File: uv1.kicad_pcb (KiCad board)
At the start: 2 copper layers, 54.9 x 63 mm, 14 parts, among them J1 Conn_02x06_Odd_Even, J2 Conn_01x02, U1 TC7106, U2 LCD-A2X1C50TR

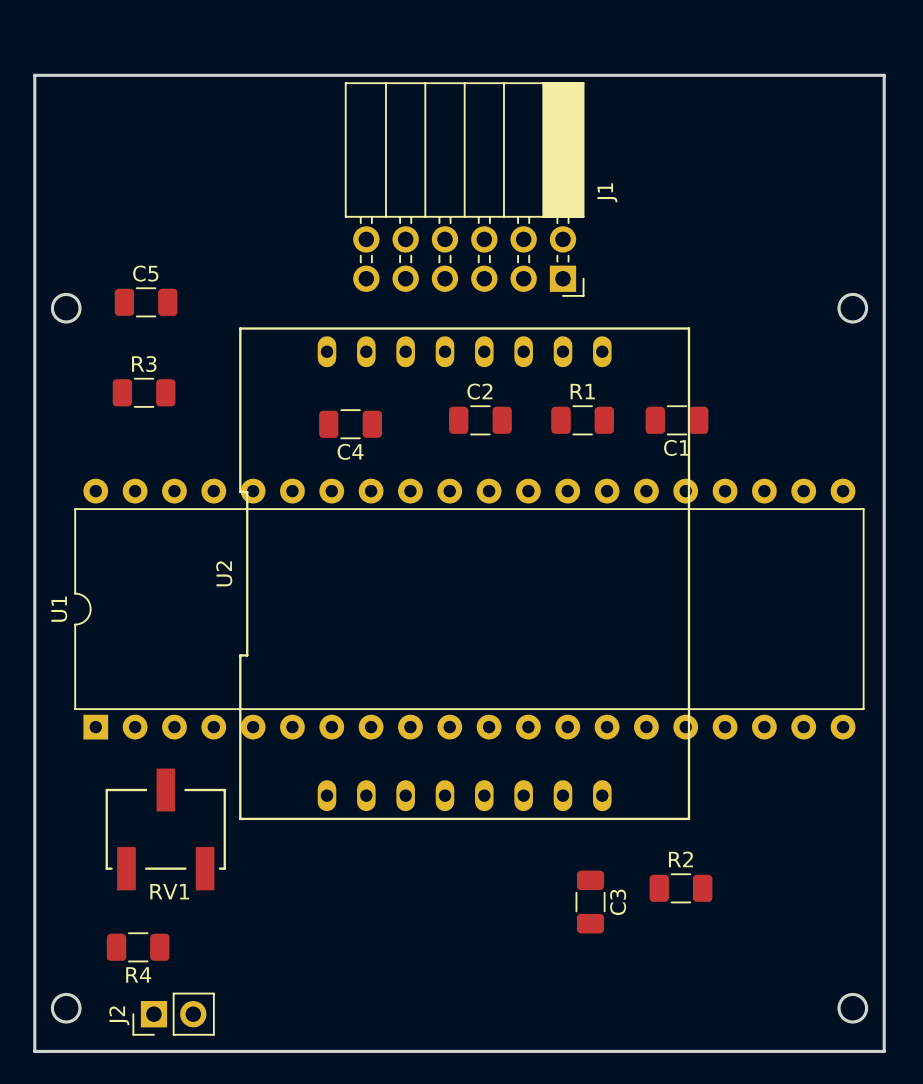
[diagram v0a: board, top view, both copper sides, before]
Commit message: Display DE151 Sensor connector 2x 2x2 male
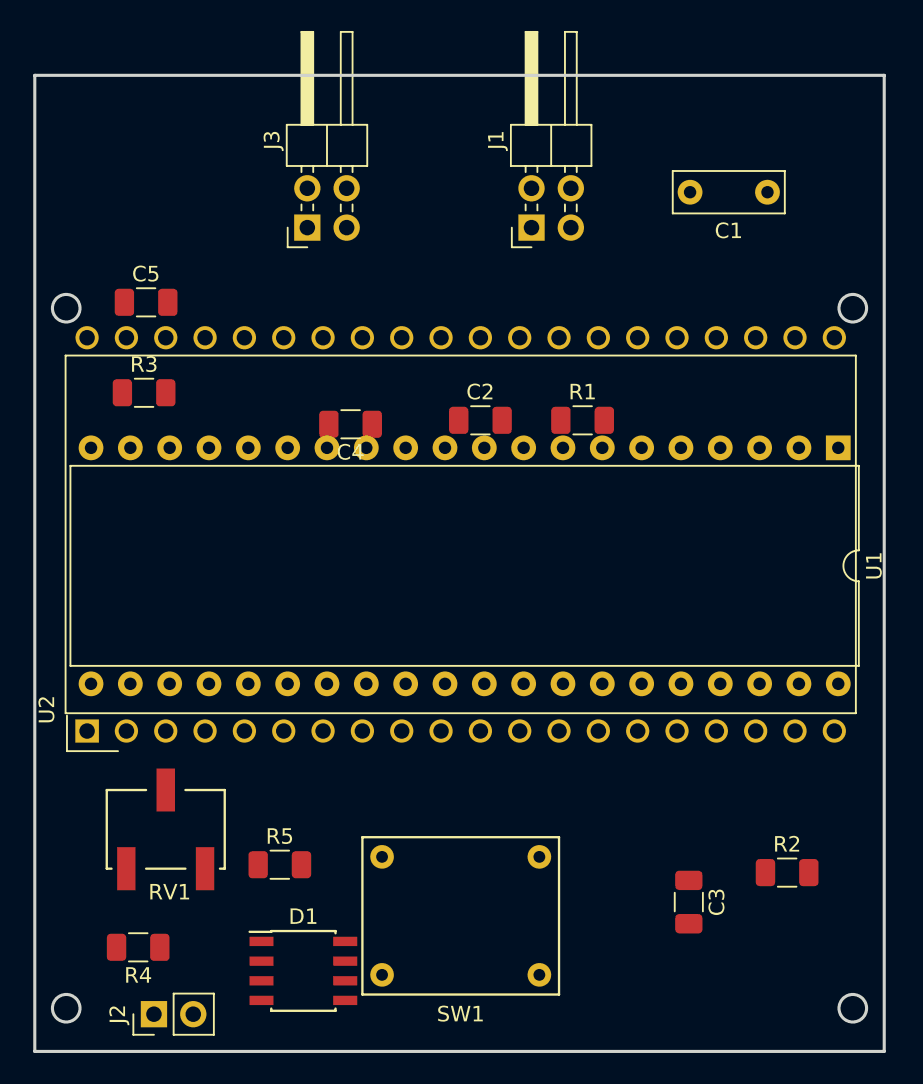
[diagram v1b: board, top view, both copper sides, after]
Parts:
- added D1: LM285D-1.2, Package_SO:SOIC-8_3.9x4.9mm_P1.27mm, F.Cu at (89.4, 139.7)
- added J3: Conn_02x02_Odd_Even, Connector_PinHeader_2.54mm:PinHeader_2x02_P2.54mm_Horizontal, F.Cu at (89.7, 91.7)
- added R5: 2.2k, Resistor_SMD:R_1206_3216Metric, F.Cu at (87.9, 132.8)
- added SW1: SW_Push, uv1:MEC_3FTH9, F.Cu at (99.6, 136.1)
- C1: footprint Capacitor_SMD:C_1206_3216Metric -> Capacitor_THT:C_Rect_L7.0mm_W2.5mm_P5.00mm
- J1: value Conn_02x06_Odd_Even -> Conn_02x02_Odd_Even; footprint Connector_PinSocket_2.54mm:PinSocket_2x06_P2.54mm_Horizontal -> Connector_PinHeader_2.54mm:PinHeader_2x02_P2.54mm_Horizontal
- R4: value 24k -> 6.8k
- RV1: value 1k -> 20k
- U2: value LCD-A2X1C50TR -> DE151-RS-20; footprint uv1:LCD-A2X1C50TR -> uv1:DE151-RS-20
- moved U1 51.2 mm to (124.0, 105.9), turned to 270 degrees
- moved U2 26.4 mm to (75.4, 124.2), turned to 90 degrees
- moved C1 15.8 mm to (119.4, 89.4)
- moved R2 6.93 mm to (120.7, 133.3)
- moved C3 6.35 mm to (114.3, 135.3)
- moved J1 3.88 mm to (104.1, 91.7), turned to 90 degrees
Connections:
- J1 pad 3: Net-(J1-Pad3) -> +9V
- J1 pad 4: Net-(J1-Pad3) -> +9V
- R2 pad 2: Net-(J1-Pad3) -> Net-(J3-Pad1)
- R4 pad 1: +9V -> Net-(R4-Pad1)
- U1 pad 1: +9V -> Net-(R4-Pad1)
- U1 pad 10: /3C -> /LCD_3C
- U1 pad 11: /3B -> /LCD_3B
- U1 pad 12: /3A -> /LCD_3A
- U1 pad 13: /3F -> /LCD_3F
- U1 pad 14: /3E -> /LCD_3E
- U1 pad 15: /2D -> /LCD_2D
- U1 pad 16: /2B -> /LCD_2B
- U1 pad 17: /2F -> /LCD_2F
- U1 pad 18: /2E -> /LCD_2E
- U1 pad 19: /1BC -> /LCD_1BC
- U1 pad 2: Net-(U1-Pad2) -> /LCD_4D
- U1 pad 20: Net-(U1-Pad20) -> /LCD_-
- U1 pad 21: /BP -> /LCD_BP
- U1 pad 22: /2G -> /LCD_2G
- U1 pad 23: /2A -> /LCD_2A
- U1 pad 24: /2C -> /LCD_2C
- U1 pad 25: /3G -> /LCD_3G
- U1 pad 3: Net-(U1-Pad3) -> /LCD_4C
- U1 pad 4: Net-(U1-Pad4) -> /LCD_4B
- U1 pad 5: Net-(U1-Pad5) -> /LCD_4A
- U1 pad 6: Net-(U1-Pad6) -> /LCD_4F
- U1 pad 7: Net-(U1-Pad7) -> /LCD_4G
- U1 pad 8: Net-(U1-Pad8) -> /LCD_4E
- U1 pad 9: /3D -> /LCD_3D
- U2 pad 1: /1BC -> /LCD_BP
- U2 pad 10: /2B -> /LCD_2D
- U2 pad 11: /2A -> /LCD_2C
- U2 pad 12: /2F -> /LCD_BP
- U2 pad 13: /2G -> /LCD_3E
- U2 pad 14: /2E -> /LCD_3D
- U2 pad 15: /2D -> /LCD_3C
- U2 pad 16: /BP -> /LCD_DP3
- U2 pad 2: /3F -> /LCD_-
- U2 pad 3: /3G -> /LCD_1BC
- U2 pad 4: /3E -> Net-(U2-Pad4)
- U2 pad 5: /3D -> Net-(U2-Pad5)
- U2 pad 6: /3C -> Net-(U2-Pad6)
- U2 pad 7: /3B -> Net-(U2-Pad7)
- U2 pad 8: /3A -> /LCD_BP
- U2 pad 9: /2C -> /LCD_2E

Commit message: DE115 LCD with new footprint + 3D
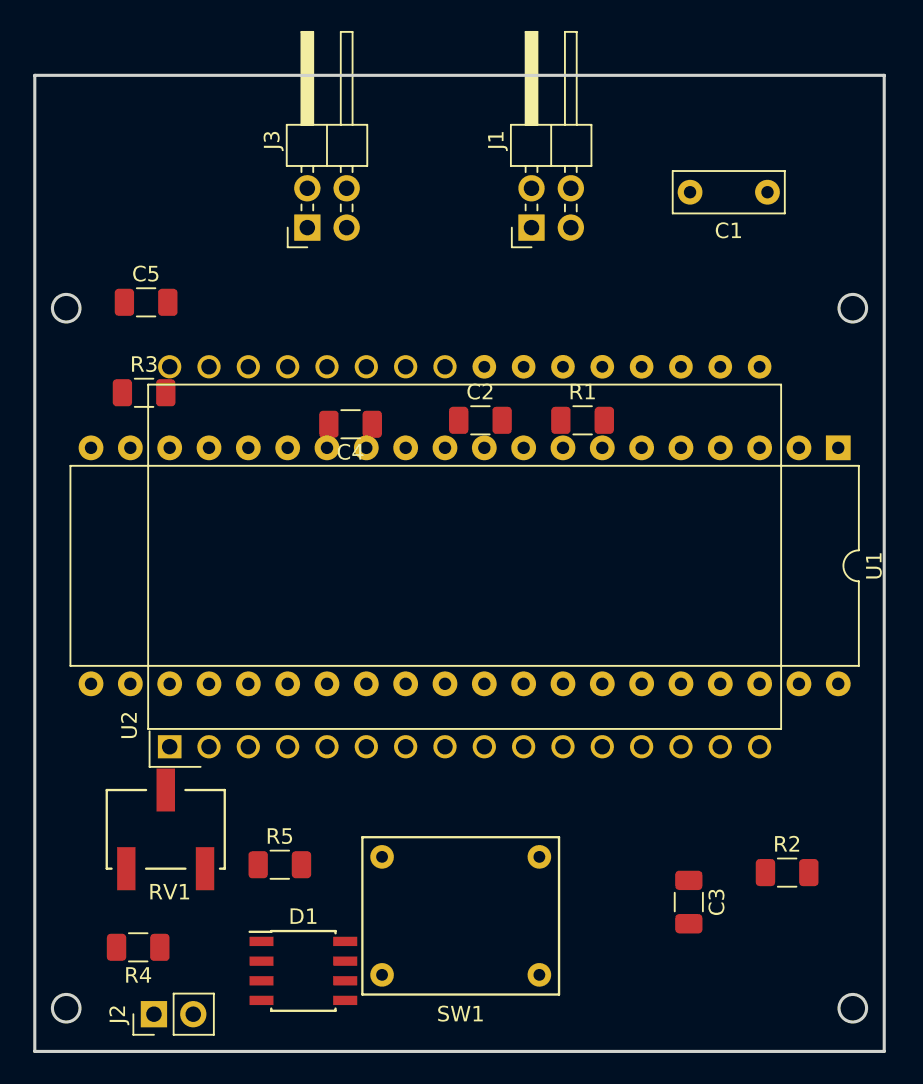
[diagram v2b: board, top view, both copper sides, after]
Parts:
- U2: value DE151-RS-20 -> DE115-RS-20; footprint uv1:DE151-RS-20 -> uv1:DE115-RS-20
- moved U2 5.43 mm to (80.8, 125.2)
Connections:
- U1 pad 10: /LCD_3C -> /LCD_2C
- U1 pad 11: /LCD_3B -> /LCD_2B
- U1 pad 12: /LCD_3A -> /LCD_2A
- U1 pad 13: /LCD_3F -> /LCD_2F
- U1 pad 14: /LCD_3E -> /LCD_2E
- U1 pad 15: /LCD_2D -> /LCD_1D
- U1 pad 16: /LCD_2B -> /LCD_1B
- U1 pad 17: /LCD_2F -> /LCD_1F
- U1 pad 18: /LCD_2E -> /LCD_1E
- U1 pad 2: /LCD_4D -> /LCD_3D
- U1 pad 22: /LCD_2G -> /LCD_1G
- U1 pad 23: /LCD_2A -> /LCD_1A
- U1 pad 24: /LCD_2C -> /LCD_1C
- U1 pad 25: /LCD_3G -> /LCD_2G
- U1 pad 3: /LCD_4C -> /LCD_3C
- U1 pad 4: /LCD_4B -> /LCD_3B
- U1 pad 5: /LCD_4A -> /LCD_3A
- U1 pad 6: /LCD_4F -> /LCD_3F
- U1 pad 7: /LCD_4G -> /LCD_3G
- U1 pad 8: /LCD_4E -> /LCD_3E
- U1 pad 9: /LCD_3D -> /LCD_2D
- U2 pad 12: /LCD_BP -> /LCD_DP3
- U2 pad 16: /LCD_DP3 -> /LCD_3B
- U2 pad 17: /LCD_4E -> (no net)
- U2 pad 18: /LCD_4D -> (no net)
- U2 pad 19: /LCD_4C -> (no net)
- U2 pad 20: /LCD_4B -> (no net)
- U2 pad 21: /LCD_4A -> (no net)
- U2 pad 22: /LCD_4F -> (no net)
- U2 pad 23: /LCD_4G -> (no net)
- U2 pad 24: /LCD_3B -> (no net)
- U2 pad 25: /LCD_3A -> /LCD_1A
- U2 pad 26: /LCD_3F -> /LCD_1F
- U2 pad 27: /LCD_3G -> /LCD_1G
- U2 pad 28: /LCD_BP -> (no net)
- U2 pad 29: /LCD_2B -> (no net)
- U2 pad 30: /LCD_2A -> /LCD_BP
- U2 pad 31: /LCD_2F -> /LCD_BP
- U2 pad 32: /LCD_2G -> /LCD_BP
- U2 pad 4: Net-(U2-Pad4) -> /LCD_BP
- U2 pad 5: Net-(U2-Pad5) -> /LCD_1E
- U2 pad 6: Net-(U2-Pad6) -> /LCD_1D
- U2 pad 7: Net-(U2-Pad7) -> /LCD_1C

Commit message: 2x7 sensor connector
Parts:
- removed J3: Conn_02x02_Odd_Even, Connector_PinHeader_2.54mm:PinHeader_2x02_P2.54mm_Horizontal
- removed R5: 2.2k, Resistor_SMD:R_1206_3216Metric
- J1: value Conn_02x02_Odd_Even -> Conn_02x07_Odd_Even; footprint Connector_PinHeader_2.54mm:PinHeader_2x02_P2.54mm_Horizontal -> Connector_PinSocket_2.54mm:PinSocket_2x07_P2.54mm_Horizontal
- moved C4 33.6 mm to (109.5, 133.3), turned to 0 degrees
- moved C2 28.0 mm to (89.2, 129.5)
- moved R1 12.7 mm to (115.3, 94.2)
- moved C5 10.5 mm to (80.3, 86.1)
- moved R3 9.97 mm to (80.3, 92.5)
- moved J1 4.49 mm to (107.2, 95.0), turned to 270 degrees
- moved C3 3.82 mm to (115.3, 131.6)
- moved R2 2.93 mm to (121.5, 130.6)
- moved U1 2.84 mm to (123.4, 103.1)
- moved U2 2.03 mm to (80.8, 123.2)
- moved RV1 1.48 mm to (79.2, 129.8)
- moved R4 1.05 mm to (77.7, 138.4)
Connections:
- R2 pad 2: Net-(J3-Pad1) -> Net-(J1-Pad11)
- U2 pad 17: (no net) -> /LCD_3A
- U2 pad 18: (no net) -> /LCD_3F
- U2 pad 19: (no net) -> /LCD_3G
- U2 pad 20: (no net) -> /LCD_2B
- U2 pad 21: (no net) -> /LCD_2A
- U2 pad 22: (no net) -> /LCD_2F
- U2 pad 23: (no net) -> /LCD_2G
- U2 pad 24: (no net) -> /LCD_1B

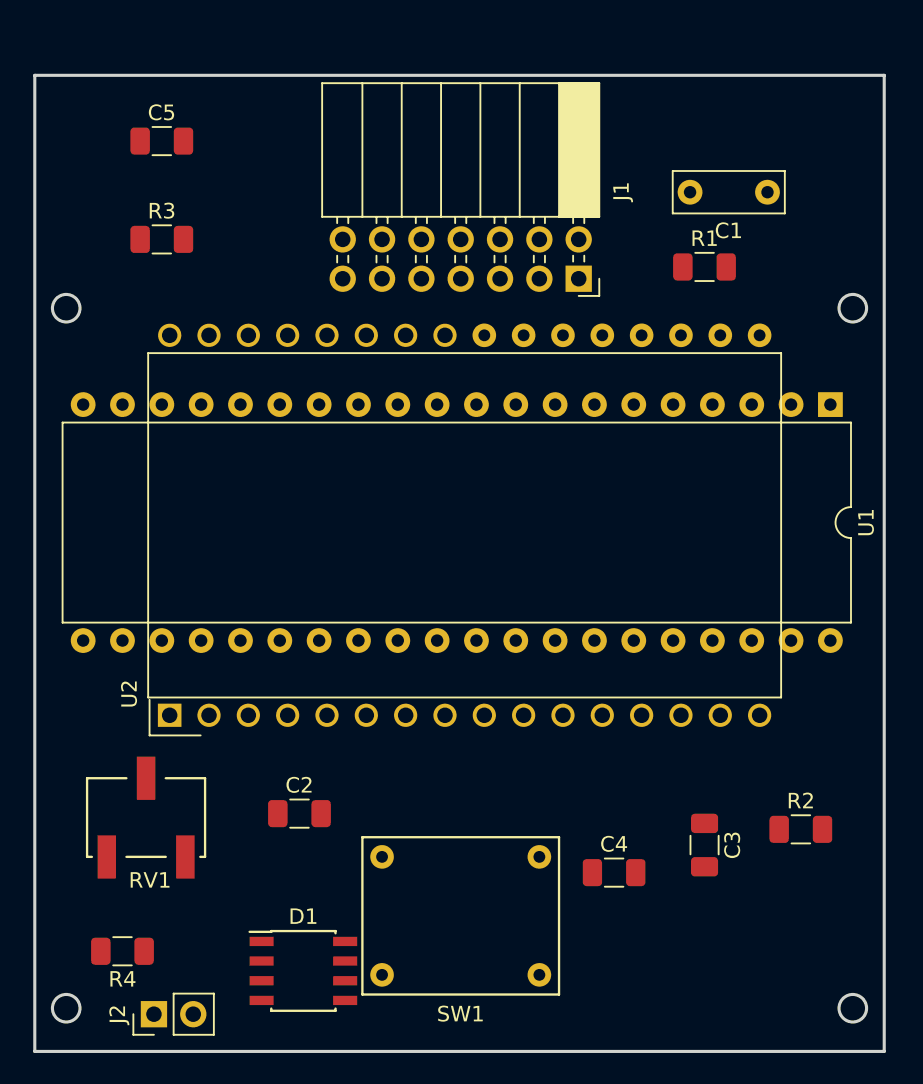
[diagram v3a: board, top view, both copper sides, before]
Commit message: Updated 3d model of LCD again
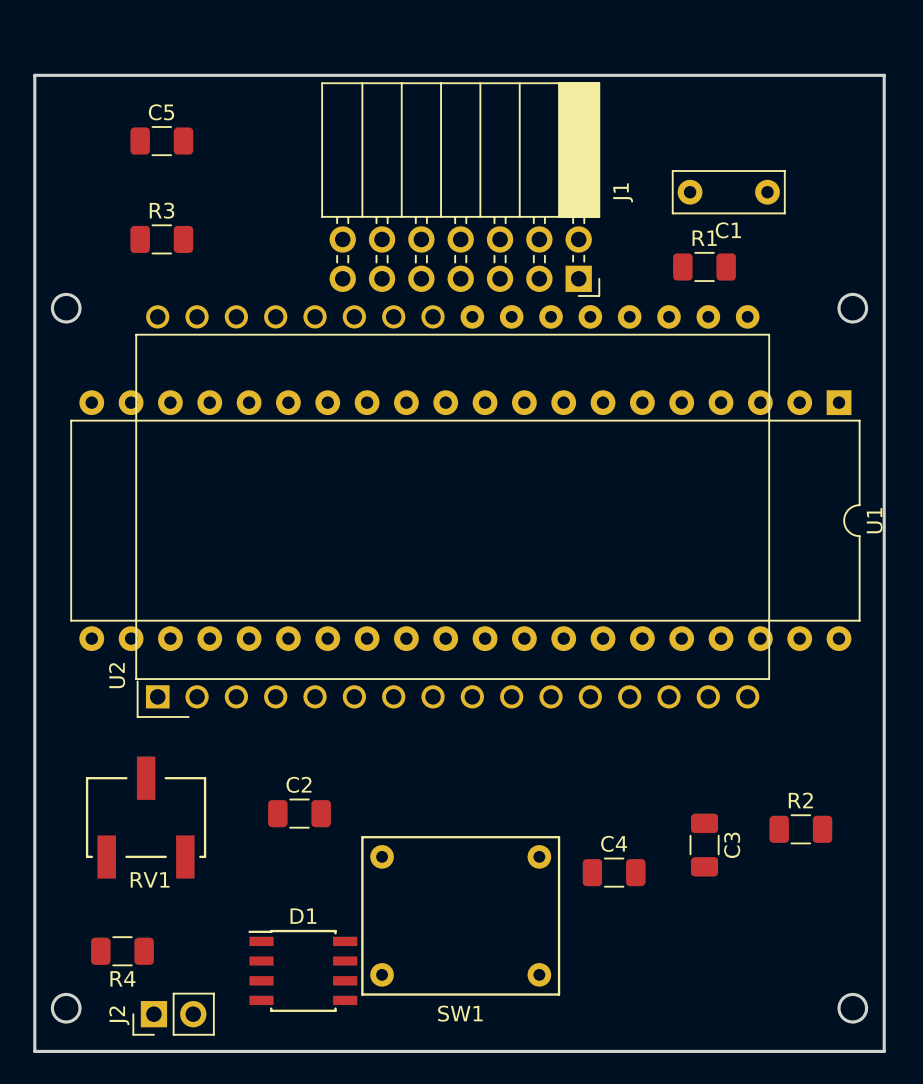
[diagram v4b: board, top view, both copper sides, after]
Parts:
- moved U2 1.42 mm to (80.0, 122.0)
- moved U1 0.57 mm to (124.0, 103.0)

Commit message: Fully routed by autorouter + tweaks
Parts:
- added JP1: Jumper_NO_Small, Connector_PinHeader_1.27mm:PinHeader_1x02_P1.27mm_Vertical, F.Cu at (122.5, 84.7)
- added R5: 470k, Resistor_SMD:R_1206_3216Metric, F.Cu at (118.6, 84.7)
- added U3: 74AHC1G04, Package_TO_SOT_SMD:SOT-23-5, F.Cu at (116.1, 103.6)
- added U4: 74HC157, Package_SO:TSSOP-16_4.4x5mm_P0.65mm, F.Cu at (107.4, 115.1)
- added U5: 74HC157, Package_SO:TSSOP-16_4.4x5mm_P0.65mm, F.Cu at (107.4, 103.6)
- J2: value Conn_01x02 -> - +; footprint Connector_PinHeader_2.54mm:PinHeader_1x02_P2.54mm_Vertical -> TestPoint:TestPoint_2Pads_Pitch2.54mm_Drill0.8mm
- U1: footprint Package_DIP:DIP-40_W15.24mm -> Package_QFP:TQFP-44_10x10mm_P0.8mm
- moved R2 50.1 mm to (80.5, 101.9), turned to 90 degrees
- moved C3 40.4 mm to (83.1, 107.2), turned to 90 degrees
- moved RV1 37.1 mm to (116.3, 129.0)
- moved C5 35.2 mm to (93.2, 118.9), turned to 180 degrees
- moved C4 33.5 mm to (83.1, 112.8), turned to 270 degrees
- moved R3 32.1 mm to (98.6, 118.9)
- moved R4 31.9 mm to (107.7, 127.5)
- moved U1 30.3 mm to (94.2, 108.5), turned to 180 degrees
- moved J2 29.9 mm to (109.5, 139.2)
- moved D1 5.40 mm to (85.9, 135.6)
- moved C2 3.02 mm to (88.0, 126.7)
- moved C1 2.62 mm to (117.1, 90.7)
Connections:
- net +9V renamed +BATT
- J2 pad 2: GND -> -BATT
- U1 pad 2: /LCD_3D -> /MUX_3D
- U1 pad 26: GND -> -BATT
- U1 pad 3: /LCD_3C -> /MUX_3C
- U1 pad 37: Net-(U1-Pad37) -> GND
- U1 pad 4: /LCD_3B -> /MUX_3B
- U1 pad 5: /LCD_3A -> /MUX_3A
- U1 pad 6: /LCD_3F -> /MUX_3F
- U1 pad 7: /LCD_3G -> /MUX_3G
- U1 pad 8: /LCD_3E -> /MUX_3E
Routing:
- net /LCD_BP: track 0.00 -> 155.3 mm, vias 0 -> 1
- net +BATT: track 0.00 -> 111.6 mm, vias 0 -> 2
- net /ACOM: track 0.00 -> 100.0 mm, vias 0 -> 1
- net Net-(C1-Pad1): track 0.00 -> 60.2 mm, vias 0 -> 1
- net GND: track 0.00 -> 59.6 mm, vias 0 -> 5
- net Net-(R1-Pad1): track 0.00 -> 50.3 mm
- net /LCD_3E: track 0.00 -> 49.9 mm, vias 0 -> 4
- net /DIGIT3_EN: track 0.00 -> 46.2 mm, vias 0 -> 2
- net Net-(C2-Pad1): track 0.00 -> 41.5 mm
- net -BATT: track 0.00 -> 40.1 mm, vias 0 -> 1
- net Net-(C1-Pad2): track 0.00 -> 35.9 mm, vias 0 -> 1
- net /LCD_1BC: track 0.00 -> 33.4 mm, vias 0 -> 2
- net Net-(RV1-Pad2): track 0.00 -> 31.9 mm, vias 0 -> 2
- net Net-(D1-Pad8): track 0.00 -> 30.7 mm
- net /LCD_DP3: track 0.00 -> 30.4 mm, vias 0 -> 1
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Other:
- net class Default: clearance 0.4 -> 0.2
- rule trace_clearance: 0.4 -> 0.2

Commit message: Decoupling caps added
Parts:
- moved J2 31.6 mm to (78.0, 137.0)
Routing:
- net +BATT: track 111.6 -> 130.0 mm
- net -BATT: track 40.1 -> 52.9 mm
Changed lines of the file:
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@@
     (thickness 1.6)
     (drawings 8)
-    (tracks 583)
+    (tracks 585)
     (zones 0)
     (modules 21)
@@
   )
   (module TestPoint:TestPoint_2Pads_Pitch2.54mm_Drill0.8mm (layer F.Cu)
-    (at 109.474 139.192 90)
+    (at 78 137 90)
     (descr "Test point with 2 pins, pitch 2.54mm, drill diameter 0.8mm")
     (tags "CONN DEV")
@@
   (via (at 110.5206 111.9433) (size 0.8) (layers F.Cu B.Cu) (net 57))
   (via (at 119.2514 114.3588) (size 0.8) (layers F.Cu B.Cu) (net 57))
+  (segment (start 82.666 132.334) (end 78 137) (width 0.4) (layer B.Cu) (net 57))
+  (segment (start 94.488 132.334) (end 82.666 132.334) (width 0.4) (layer B.Cu) (net 57))
   (segment (start 91.3379 112.1666) (end 91.3379 112.9549) (width 0.4) (layer B.Cu) (net 58))
   (segment (start 91.3379 112.9549) (end 99.066 120.683) (width 0.4) (layer B.Cu) (net 58))
@@
   (segment (start 100.6624 120.683) (end 101.59 121.6106) (width 0.4) (layer B.Cu) (net 58))
   (segment (start 101.59 121.6106) (end 101.59 125.3249) (width 0.4) (layer B.Cu) (net 58))
-  (segment (start 101.59 125.3249) (end 109.474 133.2089) (width 0.4) (layer B.Cu) (net 58))
-  (segment (start 109.474 133.2089) (end 109.474 136.652) (width 0.4) (layer B.Cu) (net 58))
   (segment (start 89.6841 106.858) (end 89.6841 107.2339) (width 0.4) (layer F.Cu) (net 58))
   (segment (start 89.6841 107.2339) (end 90.5736 108.1234) (width 0.4) (layer F.Cu) (net 58))
@@
   (segment (start 88.534 106.858) (end 89.6841 106.858) (width 0.4) (layer F.Cu) (net 58))
   (via (at 91.3379 112.1666) (size 0.8) (layers F.Cu B.Cu) (net 58))
+  (segment (start 87.1351 125.3249) (end 78 134.46) (width 0.4) (layer B.Cu) (net 58))
+  (segment (start 101.59 125.3249) (end 87.1351 125.3249) (width 0.4) (layer B.Cu) (net 58))
   (segment (start 110.392 105.257) (end 110.4016 105.2666) (width 0.4) (layer F.Cu) (net 59))
   (segment (start 110.4016 105.2666) (end 112.8517 105.2666) (width 0.4) (layer F.Cu) (net 59))

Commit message: Specified footprints for decoupling caps
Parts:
- added C6: C, Capacitor_SMD:C_1206_3216Metric, F.Cu at (110.0, 110.0)
- added C7: C, Capacitor_SMD:C_1206_3216Metric, F.Cu at (115.0, 100.0)
- added C8: C, Capacitor_SMD:C_1206_3216Metric, F.Cu at (117.0, 109.0)
- added C9: C, Capacitor_SMD:C_1206_3216Metric, F.Cu at (116.0, 113.0)
- RV1: footprint uv1:Bourns_3269W -> Potentiometer_THT:Potentiometer_Bourns_3299W_Vertical
- moved RV1 5.64 mm to (119.0, 134.0)

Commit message: Commit before rerouting
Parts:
- moved R4 7.70 mm to (100.0, 127.5)
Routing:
- net -BATT: track 52.9 -> 106.5 mm
- net Net-(C8-Pad1): track 27.4 -> 66.2 mm, vias 0 -> 1
- net /LCD_BP: track 155.3 -> 126.8 mm
- net /LCD_3E: track 49.9 -> 27.5 mm, vias 4 -> 1
- net /ACOM: track 100.0 -> 115.1 mm, vias 1 -> 0
- net Net-(C2-Pad1): track 41.5 -> 28.8 mm
- net /LCD_DP3: track 30.4 -> 18.1 mm, vias 1 -> 0
- net Net-(R1-Pad1): track 50.3 -> 38.9 mm
- net /LCD_1BC: track 33.4 -> 22.4 mm, vias 2 -> 1
- net /LCD_2E: track 29.6 -> 21.0 mm
- net /MUX_3C: track 21.7 -> 13.2 mm
- net Net-(D1-Pad8): track 30.7 -> 38.7 mm
- net /LCD_1D: track 27.2 -> 20.5 mm
- net /DIGIT3_EN: track 46.2 -> 39.5 mm
- net Net-(C1-Pad1): track 60.2 -> 66.7 mm, vias 1 -> 0
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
